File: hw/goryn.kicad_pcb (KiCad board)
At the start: 2 copper layers, 50 x 50 mm, 15 parts, among them J1 Conn_01x34, J2 Conn_01x34, J3 Conn_01x34, J4 Conn_01x34, U2 W25Q128JVS

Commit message: added DC-DC
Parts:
- added C1: 10uF, AI6YP:C_0603_1608Metric, F.Cu at (54.0, 89.5)
- added C10: 22uF, AI6YP:C_0603_1608Metric, F.Cu at (82.5, 81.4)
- added C11: 22uF, AI6YP:C_0603_1608Metric, F.Cu at (81.6, 67.4)
- added C12: 22uF, AI6YP:C_0603_1608Metric, F.Cu at (83.1, 69.0)
- added C2: 22uF, AI6YP:C_0603_1608Metric, F.Cu at (57.8, 89.4)
- added C3: 10uF, AI6YP:C_0603_1608Metric, F.Cu at (89.8, 94.8)
- added C4: 22uF, AI6YP:C_0603_1608Metric, F.Cu at (89.7, 91.2)
- added C5: 22uF, AI6YP:C_0603_1608Metric, F.Cu at (68.3, 67.7)
- added C6: 22uF, AI6YP:C_0603_1608Metric, F.Cu at (67.0, 69.0)
- added C7: 22uF, AI6YP:C_0603_1608Metric, F.Cu at (67.0, 81.5)
- added C8: 22uF, AI6YP:C_0603_1608Metric, F.Cu at (68.6, 83.0)
- added C9: 22uF, AI6YP:C_0603_1608Metric, F.Cu at (80.9, 82.8)
- added L1: 2.2uH, AI6YP:L_0805_2012Metric_Pad1.05x1.20mm_HandSolder, F.Cu at (60.3, 91.8)
- added L2: 2.2uH, AI6YP:L_0805_2012Metric_Pad1.05x1.20mm_HandSolder, F.Cu at (92.2, 89.8)
- added R10: 68K, AI6YP:R_0603_1608Metric, F.Cu at (57.6, 96.5)
- added R11: 15K, AI6YP:R_0603_1608Metric, F.Cu at (54.1, 96.4)
- added R12: 10K, AI6YP:R_0603_1608Metric, F.Cu at (96.5, 91.1)
- added R13: 15K, AI6YP:R_0603_1608Metric, F.Cu at (96.5, 94.7)
- added U3: MT3520B, AI6YP:SOT-23-5, F.Cu at (55.9, 92.7)
- added U4: MT3520B, AI6YP:SOT-23-5, F.Cu at (93.2, 94.1)
- moved R1 1.08 mm to (83.8, 80.1), turned to 135 degrees

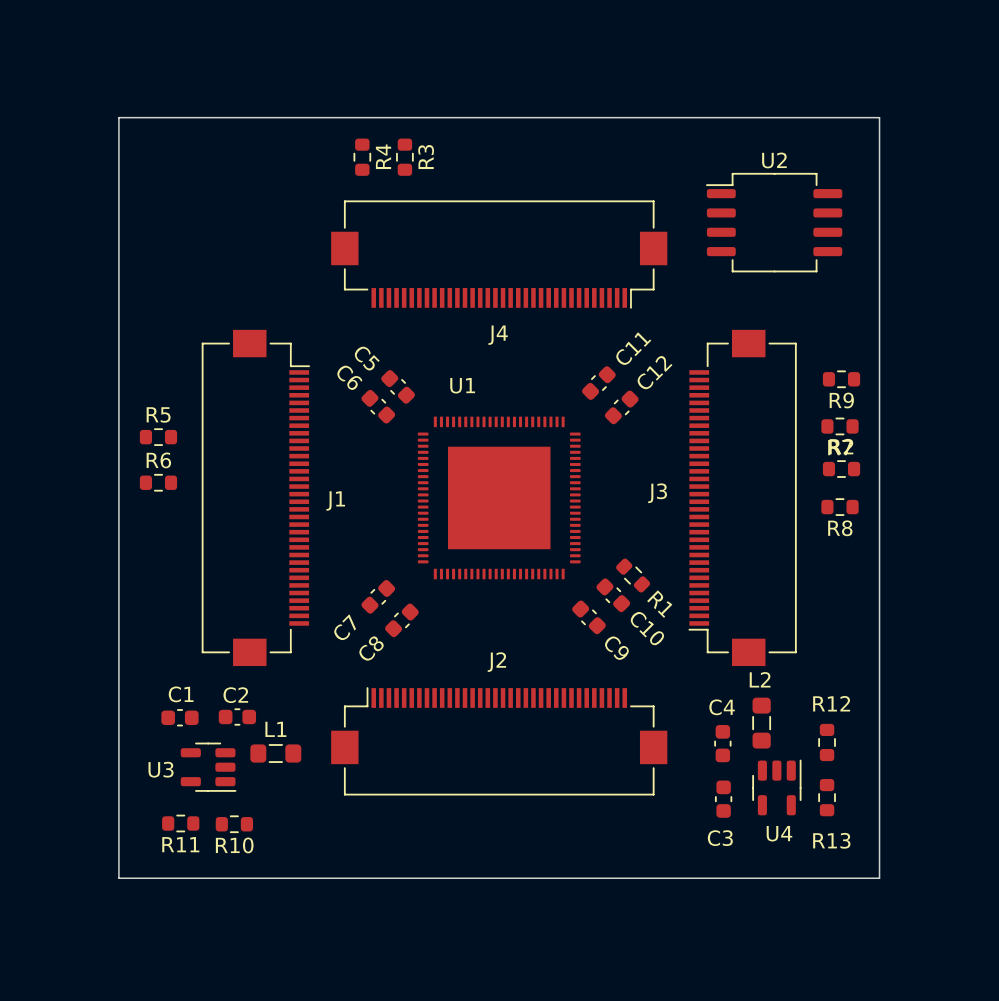
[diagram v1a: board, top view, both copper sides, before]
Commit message: FFC34 -> FFC30
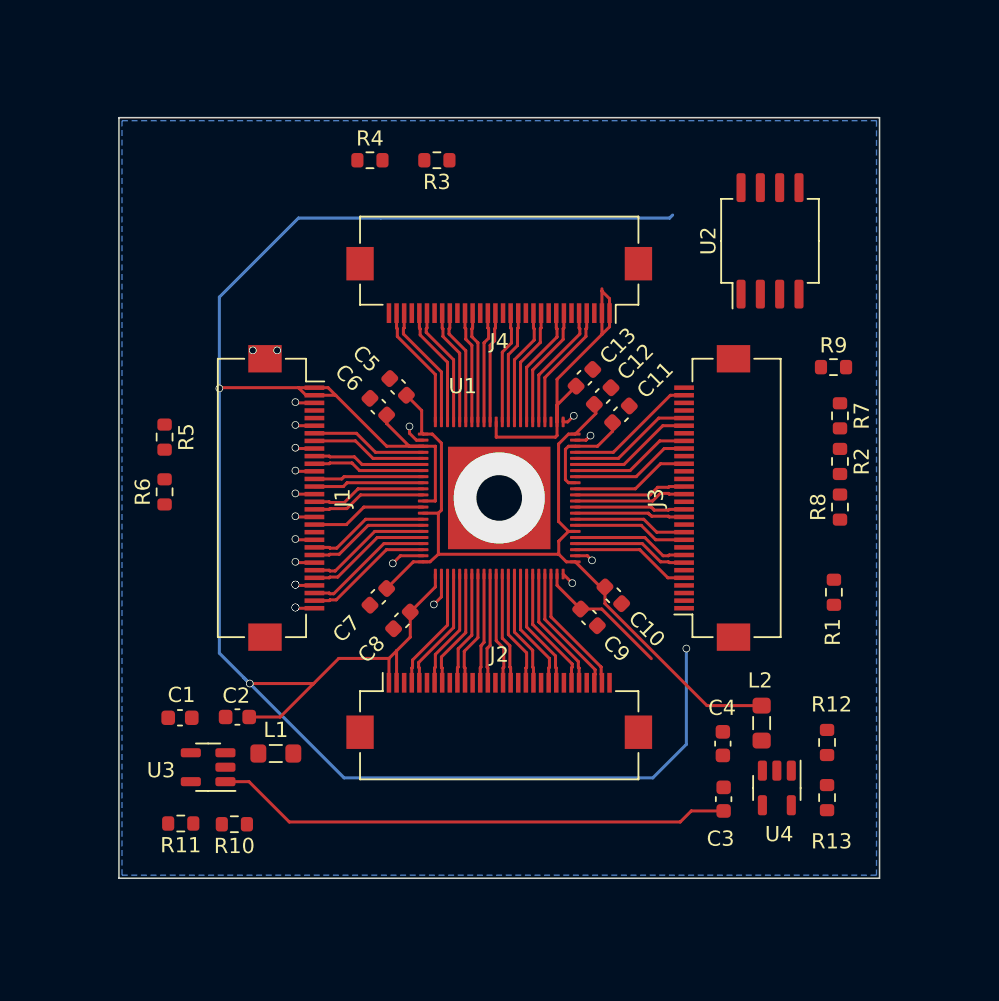
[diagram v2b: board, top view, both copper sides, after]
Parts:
- added C13: 22uF, AI6YP:C_0603_1608Metric, F.Cu at (80.6, 67.1)
- J1, J2, J3, J4: value Conn_01x34 -> Conn_FFC_30; footprint AI6YP:Hirose_FH12-34S-0.5SH_1x34-1MP_P0.50mm_Horizontal -> AI6YP:Hirose_FH12-30S-0.5SH_1x30-1MP_P0.50mm_Horizontal
- moved R1 13.2 mm to (97.0, 81.2), turned to 90 degrees
- moved C11 2.51 mm to (83.0, 69.5)
- moved R3 2.11 mm to (70.9, 52.8), turned to 180 degrees
- moved C12 1.46 mm to (81.8, 68.3)
- moved U2 1.24 mm to (92.8, 58.1), turned to 90 degrees
- moved J1 1.00 mm to (61.0, 75.0)
- moved J2 1.00 mm to (75.0, 89.0)
- moved J3 1.00 mm to (89.0, 75.0)
- moved J4 1.00 mm to (75.0, 61.0)
- moved R9 0.96 mm to (97.0, 66.4), turned to 0 degrees
- moved R6 0.72 mm to (53.0, 74.6), turned to 90 degrees
- moved R7 0.70 mm to (97.4, 69.6), turned to -90 degrees
- moved R4 0.54 mm to (66.5, 52.8), turned to 0 degrees
- moved R2 0.51 mm to (97.4, 72.6), turned to -90 degrees
- moved R5 0.40 mm to (53.0, 71.0), turned to -90 degrees
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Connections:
- J1 pad 1: GND -> +3V3
- J1 pad 10: GND -> /West/IOR26_P
- J1 pad 11: Net-(J1-Pin_11) -> /West/IOR26_N
- J1 pad 12: Net-(J1-Pin_12) -> GND
- J1 pad 13: GND -> Net-(J1-Pin_13)
- J1 pad 15: Net-(J1-Pin_15) -> GND
- J1 pad 16: GND -> /West/IOL29_P
- J1 pad 17: Net-(J1-Pin_17) -> /West/IOL29_N
- J1 pad 18: Net-(J1-Pin_18) -> GND
- J1 pad 19: GND -> Net-(J1-Pin_19)
- J1 pad 2: unconnected-(J1-Pin_2-Pad2) -> +3V3
- J1 pad 20: Net-(J1-Pin_20) -> unconnected-(J1-Pin_20-Pad20)
- J1 pad 21: unconnected-(J1-Pin_21-Pad21) -> GND
- J1 pad 22: GND -> /West/IOL47_P
- J1 pad 23: Net-(J1-Pin_23) -> /West/IOL47_N
- J1 pad 24: Net-(J1-Pin_24) -> GND
- J1 pad 25: GND -> /West/IOL49_P
- J1 pad 26: Net-(J1-Pin_26) -> /West/IOL49_N
- J1 pad 27: Net-(J1-Pin_27) -> GND
- J1 pad 28: GND -> /West/IOL51_P
- J1 pad 29: Net-(J1-Pin_29) -> /West/IOL51_N
- J1 pad 3: unconnected-(J1-Pin_3-Pad3) -> GND
- J1 pad 30: Net-(J1-Pin_30) -> GND
- J1 pad 4: GND -> unconnected-(J1-Pin_4-Pad4)
- J1 pad 6: unconnected-(J1-Pin_6-Pad6) -> GND
- J1 pad 7: GND -> Net-(J1-Pin_7)
- J1 pad 9: Net-(J1-Pin_9) -> GND
- J2 pad 1: GND -> +3V3
- J2 pad 10: GND -> /South/IOB14_P
- J2 pad 11: Net-(J2-Pin_11) -> /South/IOB14_N
- J2 pad 12: Net-(J2-Pin_12) -> GND
- J2 pad 13: GND -> /South/IOB18_P
- J2 pad 14: Net-(J2-Pin_14) -> /South/IOB18_N
- J2 pad 15: Net-(J2-Pin_15) -> GND
- J2 pad 16: GND -> /South/IOB24_P
- J2 pad 17: Net-(J2-Pin_17) -> /South/IOB24_N
- J2 pad 18: Net-(J2-Pin_18) -> GND
- J2 pad 19: GND -> /South/IOB30_P
- J2 pad 2: unconnected-(J2-Pin_2-Pad2) -> +3V3
- J2 pad 20: Net-(J2-Pin_20) -> /South/IOB30_N
- J2 pad 21: Net-(J2-Pin_21) -> GND
- J2 pad 22: GND -> /South/IOB34_P
- J2 pad 23: Net-(J2-Pin_23) -> /South/IOB34_N
- J2 pad 24: Net-(J2-Pin_24) -> GND
- J2 pad 25: GND -> /South/IOB40_P
- J2 pad 26: Net-(J2-Pin_26) -> /South/IOB40_N
- J2 pad 27: Net-(J2-Pin_27) -> GND
- J2 pad 28: GND -> /South/IOB43_P
- J2 pad 29: Net-(J2-Pin_29) -> /South/IOB43_N
- J2 pad 3: unconnected-(J2-Pin_3-Pad3) -> GND
- J2 pad 30: Net-(J2-Pin_30) -> GND
- J2 pad 4: GND -> /South/IOB6_P
- J2 pad 5: Net-(J2-Pin_5) -> /South/IOB6_N
- J2 pad 6: Net-(J2-Pin_6) -> GND
- J2 pad 7: GND -> /South/IOB8_P
- J2 pad 8: Net-(J2-Pin_8) -> /South/IOB8_N
- J2 pad 9: Net-(J2-Pin_9) -> GND
- J3 pad 1: GND -> +3V3
- J3 pad 10: GND -> Net-(J3-Pin_10)
- J3 pad 12: Net-(J3-Pin_12) -> GND
- J3 pad 13: GND -> /East/IOR38_N
- J3 pad 14: Net-(J3-Pin_14) -> /East/IOR38_P
- J3 pad 15: Net-(J3-Pin_15) -> GND
- J3 pad 16: GND -> /East/IOR36_N
- J3 pad 17: Net-(J3-Pin_17) -> /East/IOR36_P
- J3 pad 18: Net-(J3-Pin_18) -> GND
- J3 pad 19: GND -> unconnected-(J3-Pin_19-Pad19)
- J3 pad 2: unconnected-(J3-Pin_2-Pad2) -> +3V3
- J3 pad 20: unconnected-(J3-Pin_20-Pad20) -> MSPI_WP
- J3 pad 21: MSPI_WP -> GND
- J3 pad 22: GND -> MSPI_CLK
- J3 pad 23: MSPI_CLK -> MSPI_CS
- J3 pad 24: MSPI_CS -> GND
- J3 pad 25: GND -> MSPI_DI
- J3 pad 26: MSPI_DI -> MSPI_DO
- J3 pad 27: MSPI_DO -> GND
- J3 pad 28: GND -> unconnected-(J3-Pin_28-Pad28)
- J3 pad 29: unconnected-(J3-Pin_29-Pad29) -> MSPI_HOLD
- J3 pad 3: unconnected-(J3-Pin_3-Pad3) -> GND
- J3 pad 30: MSPI_HOLD -> GND
- J3 pad 4: GND -> unconnected-(J3-Pin_4-Pad4)
- J3 pad 5: unconnected-(J3-Pin_5-Pad5) -> Net-(J3-Pin_5)
- J3 pad 6: unconnected-(J3-Pin_6-Pad6) -> GND
- J3 pad 7: GND -> /East/IOR49_N
- J3 pad 8: Net-(J3-Pin_8) -> /East/IOR49_P
- J3 pad 9: Net-(J3-Pin_9) -> GND
- J4 pad 1: GND -> +3V3
- J4 pad 10: GND -> /North/IOT34_N
- J4 pad 11: Net-(J4-Pin_11) -> /North/IOT34_P
- J4 pad 12: Net-(J4-Pin_12) -> GND
- J4 pad 13: GND -> /North/IOT30_N
- J4 pad 14: Net-(J4-Pin_14) -> /North/IOT30_P
- J4 pad 15: Net-(J4-Pin_15) -> GND
- J4 pad 16: GND -> /North/IOT27_N
- J4 pad 17: Net-(J4-Pin_17) -> /North/IOT27_P
- J4 pad 18: Net-(J4-Pin_18) -> GND
- J4 pad 19: GND -> /North/IOT17_N
- J4 pad 2: unconnected-(J4-Pin_2-Pad2) -> +3V3
- J4 pad 20: Net-(J4-Pin_20) -> /North/IOT17_P
- J4 pad 21: Net-(J4-Pin_21) -> GND
- J4 pad 22: GND -> /North/IOT6_N
- J4 pad 23: Net-(J4-Pin_23) -> /North/IOT6_P
- J4 pad 24: Net-(J4-Pin_24) -> GND
- J4 pad 25: GND -> /North/IOT4_N
- J4 pad 26: Net-(J4-Pin_26) -> /North/IOT4_P
- J4 pad 27: Net-(J4-Pin_27) -> GND
- J4 pad 28: GND -> /North/IOR30_N
- J4 pad 29: Net-(J4-Pin_29) -> /North/IOR30_P
- J4 pad 3: unconnected-(J4-Pin_3-Pad3) -> GND
- J4 pad 30: Net-(J4-Pin_30) -> GND
- J4 pad 4: GND -> /North/IOT44_N
- J4 pad 5: unconnected-(J4-Pin_5-Pad5) -> /North/IOT44_P
- J4 pad 6: Net-(J4-Pin_6) -> GND
- J4 pad 7: GND -> /North/IOT40_N
- J4 pad 8: Net-(J4-Pin_8) -> /North/IOT40_P
- J4 pad 9: Net-(J4-Pin_9) -> GND
- R1 pad 2: Net-(U1C-EXTR) -> Net-(J3-Pin_5)
- R3 pad 2: Net-(J4-Pin_32) -> /North/IOR30_N
- R4 pad 2: Net-(J4-Pin_33) -> /North/IOR30_P
- R5 pad 2: Net-(J1-Pin_11) -> /West/IOR26_P
- R6 pad 2: Net-(J1-Pin_14) -> Net-(J1-Pin_13)
- U1 pad 10: Net-(J1-Pin_17) -> /West/IOL29_P
- U1 pad 11: Net-(J1-Pin_18) -> /West/IOL29_N
- U1 pad 13: Net-(J1-Pin_20) -> Net-(J1-Pin_19)
- U1 pad 15: Net-(J1-Pin_23) -> /West/IOL47_P
- U1 pad 16: Net-(J1-Pin_24) -> /West/IOL47_N
- U1 pad 17: Net-(J1-Pin_26) -> /West/IOL49_P
- U1 pad 18: Net-(J1-Pin_27) -> /West/IOL49_N
- U1 pad 19: Net-(J1-Pin_29) -> /West/IOL51_P
- U1 pad 20: Net-(J1-Pin_30) -> /West/IOL51_N
- U1 pad 25: Net-(J2-Pin_5) -> /South/IOB6_P
- U1 pad 26: Net-(J2-Pin_6) -> /South/IOB6_N
- U1 pad 27: Net-(J2-Pin_8) -> /South/IOB8_P
- U1 pad 28: Net-(J2-Pin_9) -> /South/IOB8_N
- U1 pad 29: Net-(J2-Pin_11) -> /South/IOB14_P
- U1 pad 30: Net-(J2-Pin_12) -> /South/IOB14_N
- U1 pad 31: Net-(J2-Pin_14) -> /South/IOB18_P
- U1 pad 32: Net-(J2-Pin_15) -> /South/IOB18_N
- U1 pad 33: Net-(J2-Pin_17) -> /South/IOB24_P
- U1 pad 34: Net-(J2-Pin_18) -> /South/IOB24_N
- U1 pad 35: Net-(J2-Pin_20) -> /South/IOB30_P
- U1 pad 36: Net-(J2-Pin_21) -> /South/IOB30_N
- U1 pad 37: Net-(J2-Pin_23) -> /South/IOB34_P
- U1 pad 38: Net-(J2-Pin_24) -> /South/IOB34_N
- U1 pad 39: Net-(J2-Pin_26) -> /South/IOB40_P
- U1 pad 4: Net-(J1-Pin_8) -> Net-(J1-Pin_7)
- U1 pad 40: Net-(J2-Pin_27) -> /South/IOB40_N
- U1 pad 41: Net-(J2-Pin_29) -> /South/IOB43_P
- U1 pad 42: Net-(J2-Pin_30) -> /South/IOB43_N
- U1 pad 43: GND -> +3V3
- U1 pad 44: +3V3 -> GND
- U1 pad 47: Net-(U1C-EXTR) -> Net-(J3-Pin_5)
- U1 pad 48: Net-(J3-Pin_8) -> /East/IOR49_N
- U1 pad 49: Net-(J3-Pin_9) -> /East/IOR49_P
- U1 pad 5: Net-(J1-Pin_9) -> Net-(J1-Pin_8)
- U1 pad 51: Net-(J3-Pin_11) -> Net-(J3-Pin_10)
- U1 pad 52: Net-(J3-Pin_12) -> Net-(J3-Pin_11)
- U1 pad 53: Net-(J3-Pin_14) -> /East/IOR38_N
- U1 pad 54: Net-(J3-Pin_15) -> /East/IOR38_P
- U1 pad 55: Net-(J3-Pin_17) -> /East/IOR36_N
- U1 pad 56: Net-(J3-Pin_18) -> /East/IOR36_P
- U1 pad 6: Net-(J1-Pin_11) -> /West/IOR26_P
- U1 pad 67: +3V3 -> GND
- U1 pad 68: GND -> +3V3
- U1 pad 69: Net-(J4-Pin_6) -> unconnected-(U1D-IOT50A-Pad69)
- U1 pad 7: Net-(J1-Pin_12) -> /West/IOR26_N
- U1 pad 70: Net-(J4-Pin_8) -> /North/IOT44_N
- U1 pad 71: Net-(J4-Pin_9) -> /North/IOT44_P
- U1 pad 72: Net-(J4-Pin_11) -> /North/IOT40_N
- U1 pad 73: Net-(J4-Pin_12) -> /North/IOT40_P
- U1 pad 74: Net-(J4-Pin_14) -> /North/IOT34_N
- U1 pad 75: Net-(J4-Pin_15) -> /North/IOT34_P
- U1 pad 76: Net-(J4-Pin_17) -> /North/IOT30_N
- U1 pad 77: Net-(J4-Pin_18) -> /North/IOT30_P
- U1 pad 79: Net-(J4-Pin_20) -> /North/IOT27_N
- U1 pad 8: Net-(J1-Pin_14) -> Net-(J1-Pin_13)
- U1 pad 80: Net-(J4-Pin_21) -> /North/IOT27_P
- U1 pad 81: Net-(J4-Pin_23) -> /North/IOT17_N
- U1 pad 82: Net-(J4-Pin_24) -> /North/IOT17_P
- U1 pad 83: Net-(J4-Pin_26) -> /North/IOT6_N
- U1 pad 84: Net-(J4-Pin_27) -> /North/IOT6_P
- U1 pad 85: Net-(J4-Pin_29) -> /North/IOT4_N
- U1 pad 86: Net-(J4-Pin_30) -> /North/IOT4_P
- U1 pad 87: Net-(J4-Pin_32) -> /North/IOR30_N
- U1 pad 88: Net-(J4-Pin_33) -> /North/IOR30_P
- U1 pad 9: Net-(J1-Pin_15) -> Net-(J1-Pin_14)
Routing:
- net +3V3: track 0.00 -> 187.2 mm, vias 0 -> 3
- net +1V0: track 0.00 -> 55.2 mm
- net +5V: track 0.00 -> 34.1 mm
- net GND: track 0.00 -> 23.5 mm, vias 0 -> 22
- net MSPI_HOLD: track 0.00 -> 8.70 mm
- net /South/IOB43_P: track 0.00 -> 8.54 mm
- net /South/IOB43_N: track 0.00 -> 8.54 mm
- net /West/IOL51_N: track 0.00 -> 8.54 mm
- net /West/IOL51_P: track 0.00 -> 8.54 mm
- net /North/IOT44_N: track 0.00 -> 8.29 mm
- net /North/IOT44_P: track 0.00 -> 8.29 mm
- net /South/IOB40_N: track 0.00 -> 8.25 mm
- net MSPI_DO: track 0.00 -> 8.25 mm
- net /West/IOL49_N: track 0.00 -> 8.25 mm
- net /South/IOB40_P: track 0.00 -> 8.25 mm
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- added copper zone on B.Cu, net GND
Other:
- rule pad_to_mask_clearance: 0 -> 0.04

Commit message: happy kicad 8
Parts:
- added C14: 1uF, AI6YP:C_0603_1608Metric, F.Cu at (63.4, 60.2)
- added H1: MountingHole_M3, AI6YP:MountingHole_3.2mm_M3_Pad_Via, F.Cu at (50.0, 75.0)
- added H2: MountingHole_M3, AI6YP:MountingHole_3.2mm_M3_Pad_Via, F.Cu at (75.0, 100.0)
- added H3: MountingHole_M3, AI6YP:MountingHole_3.2mm_M3_Pad_Via, F.Cu at (100.0, 75.0)
- added H4: MountingHole_M3, AI6YP:MountingHole_3.2mm_M3_Pad_Via, F.Cu at (75.0, 50.0)
- added J5: Conn_Coaxial, AI6YP:U.FL_Hirose_U.FL-R-SMT-1_Vertical, F.Cu at (53.4, 53.9)
- added J6: USB_C_Receptacle_USB2.0_16P, AI6YP:USB_C_Receptacle_GCT_USB4105-xx-A_16P_TopMnt_Horizontal, F.Cu at (56.4, 96.3)
- added R14: 22, AI6YP:R_0603_1608Metric, F.Cu at (56.7, 63.0)
- added R15: 22, AI6YP:R_0603_1608Metric, F.Cu at (53.4, 57.5)
- added R16: 0R, AI6YP:R_0603_1608Metric, F.Cu at (53.8, 84.6)
- added R17: 0R, AI6YP:R_0603_1608Metric, F.Cu at (52.2, 84.6)
- added R18: 5.1K, AI6YP:R_0603_1608Metric, F.Cu at (51.7, 89.7)
- added R19: 5.1K, AI6YP:R_0603_1608Metric, F.Cu at (63.7, 98.6)
- added X1: osc_4pin_3.2_2.5, AI6YP:Crystal_SMD_EuroQuartz_MT-4Pin_3.2x2.5mm_HandSoldering, F.Cu at (58.7, 58.5)
- moved R2 19.6 mm to (87.7, 55.6), turned to 90 degrees
- moved R1 13.0 mm to (84.1, 80.0), turned to 135 degrees
- moved R6 12.4 mm to (52.0, 62.2), turned to -90 degrees
- moved R9 11.8 mm to (87.7, 59.1), turned to -90 degrees
- moved R8 10.5 mm to (97.2, 65.1), turned to 180 degrees
- moved R11 9.61 mm to (63.7, 96.3), turned to 0 degrees
- moved R5 8.84 mm to (53.8, 62.2)
- moved R3 7.65 mm to (63.3, 52.2), turned to 0 degrees
- moved R7 7.62 mm to (96.8, 62.0), turned to 0 degrees
- moved C1 6.98 mm to (60.9, 90.4)
- moved R10 6.44 mm to (63.2, 93.3), turned to -90 degrees
- moved L1 4.90 mm to (61.3, 87.0)
- moved U3 4.46 mm to (56.6, 88.3)
- moved C2 3.59 mm to (61.3, 88.8)
- moved R4 3.41 mm to (63.3, 53.9)
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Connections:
- J1 pad 10: /West/IOR26_P -> /West/IOR26_N
- J1 pad 11: /West/IOR26_N -> GND
- J1 pad 12: GND -> Net-(J1-Pin_12)
- J1 pad 14: Net-(J1-Pin_14) -> GND
- J1 pad 15: GND -> /West/IOL29_P
- J1 pad 16: /West/IOL29_P -> /West/IOL29_N
- J1 pad 17: /West/IOL29_N -> GND
- J1 pad 18: GND -> Net-(J1-Pin_18)
- J1 pad 19: Net-(J1-Pin_19) -> unconnected-(J1-Pin_19-Pad19)
- J1 pad 2: +3V3 -> GND
- J1 pad 20: unconnected-(J1-Pin_20-Pad20) -> GND
- J1 pad 21: GND -> /West/IOL47_P
- J1 pad 22: /West/IOL47_P -> /West/IOL47_N
- J1 pad 23: /West/IOL47_N -> GND
- J1 pad 24: GND -> /West/IOL49_P
- J1 pad 25: /West/IOL49_P -> /West/IOL49_N
- J1 pad 26: /West/IOL49_N -> GND
- J1 pad 27: GND -> /West/IOL51_P
- J1 pad 28: /West/IOL51_P -> /West/IOL51_N
- J1 pad 29: /West/IOL51_N -> GND
- J1 pad 3: GND -> unconnected-(J1-Pin_3-Pad3)
- J1 pad 30: GND -> +3V3
- J1 pad 5: unconnected-(J1-Pin_5-Pad5) -> GND
- J1 pad 6: GND -> Net-(J1-Pin_6)
- J1 pad 8: Net-(J1-Pin_8) -> GND
- J1 pad 9: GND -> /West/IOR26_P
- J2 pad 10: /South/IOB14_P -> /South/IOB14_N
- J2 pad 11: /South/IOB14_N -> GND
- J2 pad 12: GND -> /South/IOB18_P
- J2 pad 13: /South/IOB18_P -> /South/IOB18_N
- J2 pad 14: /South/IOB18_N -> GND
- J2 pad 15: GND -> /South/IOB24_P
- J2 pad 16: /South/IOB24_P -> /South/IOB24_N
- J2 pad 17: /South/IOB24_N -> GND
- J2 pad 18: GND -> /South/IOB30_P
- J2 pad 19: /South/IOB30_P -> /South/IOB30_N
- J2 pad 2: +3V3 -> GND
- J2 pad 20: /South/IOB30_N -> GND
- J2 pad 21: GND -> /South/IOB34_P
- J2 pad 22: /South/IOB34_P -> /South/IOB34_N
- J2 pad 23: /South/IOB34_N -> GND
- J2 pad 24: GND -> /South/IOB40_P
- J2 pad 25: /South/IOB40_P -> /South/IOB40_N
- J2 pad 26: /South/IOB40_N -> GND
- J2 pad 27: GND -> /South/IOB43_P
- J2 pad 28: /South/IOB43_P -> /South/IOB43_N
- J2 pad 29: /South/IOB43_N -> GND
- J2 pad 3: GND -> /South/IOB6_P
- J2 pad 30: GND -> +3V3
- J2 pad 4: /South/IOB6_P -> /South/IOB6_N
- J2 pad 5: /South/IOB6_N -> GND
- J2 pad 6: GND -> /South/IOB8_P
- J2 pad 7: /South/IOB8_P -> /South/IOB8_N
- J2 pad 8: /South/IOB8_N -> GND
- J2 pad 9: GND -> /South/IOB14_P
- J3 pad 11: Net-(J3-Pin_11) -> GND
- J3 pad 12: GND -> /East/IOR38_N
- J3 pad 13: /East/IOR38_N -> /East/IOR38_P
- J3 pad 14: /East/IOR38_P -> GND
- J3 pad 15: GND -> /East/IOR36_N
- J3 pad 16: /East/IOR36_N -> /East/IOR36_P
- J3 pad 17: /East/IOR36_P -> GND
- J3 pad 18: GND -> unconnected-(J3-Pin_18-Pad18)
- J3 pad 19: unconnected-(J3-Pin_19-Pad19) -> MSPI_WP
- J3 pad 2: +3V3 -> GND
- J3 pad 20: MSPI_WP -> GND
- J3 pad 21: GND -> MSPI_CLK
- J3 pad 22: MSPI_CLK -> MSPI_CS
- J3 pad 23: MSPI_CS -> GND
- J3 pad 24: GND -> MSPI_DI
- J3 pad 25: MSPI_DI -> MSPI_DO
- J3 pad 26: MSPI_DO -> GND
- J3 pad 27: GND -> unconnected-(J3-Pin_27-Pad27)
- J3 pad 28: unconnected-(J3-Pin_28-Pad28) -> MSPI_HOLD
- J3 pad 29: MSPI_HOLD -> GND
- J3 pad 3: GND -> unconnected-(J3-Pin_3-Pad3)
- J3 pad 30: GND -> +3V3
- J3 pad 5: Net-(J3-Pin_5) -> GND
- J3 pad 6: GND -> /East/IOR49_N
- J3 pad 7: /East/IOR49_N -> /East/IOR49_P
- J3 pad 8: /East/IOR49_P -> GND
- J3 pad 9: GND -> Net-(J3-Pin_9)
- J4 pad 10: /North/IOT34_N -> /North/IOT34_P
- J4 pad 11: /North/IOT34_P -> GND
- J4 pad 12: GND -> /North/IOT30_N
- J4 pad 13: /North/IOT30_N -> /North/IOT30_P
- J4 pad 14: /North/IOT30_P -> GND
- J4 pad 15: GND -> /North/IOT27_N
- J4 pad 16: /North/IOT27_N -> /North/IOT27_P
- J4 pad 17: /North/IOT27_P -> GND
- J4 pad 18: GND -> /North/IOT17_N
- J4 pad 19: /North/IOT17_N -> /North/IOT17_P
- J4 pad 2: +3V3 -> GND
- J4 pad 20: /North/IOT17_P -> GND
- J4 pad 21: GND -> /North/IOT6_N
- J4 pad 22: /North/IOT6_N -> /North/IOT6_P
- J4 pad 23: /North/IOT6_P -> GND
- J4 pad 24: GND -> /North/IOT4_N
- J4 pad 25: /North/IOT4_N -> /North/IOT4_P
- J4 pad 26: /North/IOT4_P -> GND
- J4 pad 27: GND -> /North/IOR30_N
- J4 pad 28: /North/IOR30_N -> /North/IOR30_P
- J4 pad 29: /North/IOR30_P -> GND
- J4 pad 3: GND -> /North/IOT44_N
- J4 pad 30: GND -> +3V3
- J4 pad 4: /North/IOT44_N -> /North/IOT44_P
- J4 pad 5: /North/IOT44_P -> GND
- J4 pad 6: GND -> /North/IOT40_N
- J4 pad 7: /North/IOT40_N -> /North/IOT40_P
- J4 pad 8: /North/IOT40_P -> GND
- J4 pad 9: GND -> /North/IOT34_N
- R1 pad 2: Net-(J3-Pin_5) -> Net-(U1C-EXTR)
- R6 pad 2: Net-(J1-Pin_13) -> Net-(J1-Pin_12)
- U1 pad 13: Net-(J1-Pin_19) -> Net-(J1-Pin_18)
- U1 pad 4: Net-(J1-Pin_7) -> Net-(J1-Pin_6)
- U1 pad 43: +3V3 -> GND
- U1 pad 44: GND -> +3V3
- U1 pad 47: Net-(J3-Pin_5) -> Net-(U1C-EXTR)
- U1 pad 5: Net-(J1-Pin_8) -> Net-(J1-Pin_7)
- U1 pad 51: Net-(J3-Pin_10) -> Net-(J3-Pin_9)
- U1 pad 52: Net-(J3-Pin_11) -> Net-(J3-Pin_10)
- U1 pad 67: GND -> +3V3
- U1 pad 68: +3V3 -> GND
- U1 pad 8: Net-(J1-Pin_13) -> Net-(J1-Pin_12)
- U1 pad 9: Net-(J1-Pin_14) -> Net-(J1-Pin_13)
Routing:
- net MSPI_CLK: track 7.92 -> 42.9 mm
- net GND: track 23.5 -> 57.9 mm, vias 22 -> 42
- net +5V: track 34.1 -> 65.8 mm, vias 0 -> 3
- net MSPI_WP: track 7.83 -> 34.5 mm
- net Net-(J1-Pin_6): track 0.00 -> 24.7 mm
- net Net-(J1-Pin_12): track 0.00 -> 23.2 mm
- net MSPI_DI: track 8.21 -> 31.3 mm, vias 0 -> 2
- net MSPI_DO: track 8.25 -> 28.9 mm
- net MSPI_CS: track 7.96 -> 27.4 mm
- net MSPI_HOLD: track 8.70 -> 28.0 mm
- net /West/IOR26_P: track 7.38 -> 21.3 mm
- net /North/IOR30_N: track 8.21 -> 21.7 mm
- net Net-(J6-D+-PadA6): track 0.00 -> 13.4 mm
- net /North/IOR30_P: track 8.21 -> 20.4 mm
- net /West/IOL51_P: track 8.54 -> 20.6 mm
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- added copper zone on F.Cu, net GND

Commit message: finished routing
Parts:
- removed C2, C4, C7: 22uF, AI6YP:C_0603_1608Metric
- removed C3: 10uF, AI6YP:C_0603_1608Metric
- removed H1, H2, H3, H4: MountingHole_M3, AI6YP:MountingHole_3.2mm_M3_Pad_Via
- removed L1, L2: 2.2uH, AI6YP:L_0805_2012Metric_Pad1.05x1.20mm_HandSolder
- removed R16, R17: 0R, AI6YP:R_0603_1608Metric
- removed R18, R19: 5.1K, AI6YP:R_0603_1608Metric
- added C31: 10uF, AI6YP:C_0603_1608Metric, F.Cu at (59.0, 98.5)
- added C32: 22uF, AI6YP:C_0603_1608Metric, F.Cu at (66.0, 84.0)
- added C41: 10uF, AI6YP:C_0603_1608Metric, F.Cu at (90.5, 96.3)
- added C42: 22uF, AI6YP:C_0603_1608Metric, F.Cu at (91.0, 87.5)
- added J10: 3V3, AI6YP:PinHeader_1x02_P2.54mm_Vertical, F.Cu at (52.0, 62.5)
- added J30: EMI-shield-clip-corner, AI6YP:EMI-shield-clip-corner, F.Cu at (51.0, 51.0)
- added J31: EMI-shield-clip-corner, AI6YP:EMI-shield-clip-corner, F.Cu at (51.0, 99.0)
- added J32: EMI-shield-clip-corner, AI6YP:EMI-shield-clip-corner, F.Cu at (99.0, 99.0)
- added J33: EMI-shield-clip-corner, AI6YP:EMI-shield-clip-corner, F.Cu at (99.0, 51.0)
- added J8: 5V, AI6YP:PinHeader_1x02_P2.54mm_Vertical, F.Cu at (87.5, 98.0)
- added J9: 1V, AI6YP:PinHeader_1x02_P2.54mm_Vertical, F.Cu at (98.0, 87.5)
- added L31: 2.2uH, AI6YP:L_0805_2012Metric_Pad1.05x1.20mm_HandSolder, F.Cu at (60.7, 87.5)
- added L41: 2.2uH, AI6YP:L_0805_2012Metric_Pad1.05x1.20mm_HandSolder, F.Cu at (87.5, 89.0)
- added R31: 68K, AI6YP:R_0603_1608Metric, F.Cu at (63.6, 90.2)
- added R32: 15K, AI6YP:R_0603_1608Metric, F.Cu at (63.6, 93.7)
- added R41: 10K, AI6YP:R_0603_1608Metric, F.Cu at (95.5, 92.0)
- added R42: 15K, AI6YP:R_0603_1608Metric, F.Cu at (95.5, 95.5)
- C1: value 10uF -> 22uF
- R10: value 68K -> 5.1K
- R11: value 15K -> 5.1K
- R12: value 10K -> 0R
- R13: value 15K -> 0R
- moved R12 36.3 mm to (60.5, 95.5), turned to 0 degrees
- moved R13 36.1 mm to (60.5, 97.0), turned to 0 degrees
- moved R11 15.8 mm to (53.5, 84.2), turned to 90 degrees
- moved R10 12.3 mm to (55.0, 84.2), turned to 90 degrees
- moved C1 11.6 mm to (67.0, 80.5), turned to -135 degrees
- moved R8 7.24 mm to (90.3, 63.0), turned to 0 degrees
- moved R7 6.59 mm to (90.3, 61.1)
- moved R15 6.47 mm to (58.5, 61.5), turned to -90 degrees
- moved J6 5.88 mm to (53.0, 91.5), turned to -90 degrees
- moved U3 5.59 mm to (61.0, 91.7), turned to -90 degrees
- moved R5 5.22 mm to (55.3, 67.2)
- moved R6 5.22 mm to (53.5, 67.2)
- moved X1 4.52 mm to (60.6, 54.4)
- moved R14 4.11 mm to (60.5, 61.5), turned to -90 degrees
- moved J5 3.18 mm to (54.0, 57.0), turned to 180 degrees
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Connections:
- net /South/IOB43_N renamed Net-(J2-Pin_28)
- net /South/IOB43_P renamed Net-(J2-Pin_27)
- C1 pad 1: +5V -> +1V0
- J3 pad 18: unconnected-(J3-Pin_18-Pad18) -> MSPI_WP
- J3 pad 19: MSPI_WP -> unconnected-(J3-Pin_19-Pad19)
- R10 pad 1: +3V3 -> Net-(J6-CC1)
- R10 pad 2: Net-(U3-FB) -> GND
- R11 pad 1: Net-(U3-FB) -> Net-(J6-CC2)
- R12 pad 1: +1V0 -> Net-(J6-D--PadA7)
- R12 pad 2: Net-(U4-FB) -> /South/IOB6_P
- R13 pad 1: Net-(U4-FB) -> Net-(J6-D+-PadA6)
- R13 pad 2: GND -> /South/IOB6_N
- R15 pad 1: Net-(J1-Pin_6) -> Net-(J5-In)
- R15 pad 2: Net-(J5-In) -> Net-(J1-Pin_6)
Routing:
- net GND: track 57.9 -> 2.40 mm, vias 42 -> 178
- net +5V: track 65.8 -> 15.9 mm, vias 3 -> 8
- net +3V3: track 199.2 -> 150.6 mm, vias 12 -> 14
- net /South/IOB6_N: track 8.33 -> 23.6 mm
- net /South/IOB6_P: track 8.33 -> 23.4 mm
- net /West/IOL51_P: track 20.6 -> 8.33 mm
- net /West/IOL51_N: track 19.3 -> 8.33 mm
- net MSPI_WP: track 34.5 -> 43.2 mm, vias 0 -> 2
- net Net-(U3-FB): track 10.7 -> 3.69 mm
- net MSPI_CLK: track 42.9 -> 48.9 mm
- net MSPI_CS: track 27.4 -> 32.7 mm, vias 0 -> 2
- net Net-(J5-In): track 0.00 -> 5.34 mm
- net MSPI_HOLD: track 28.0 -> 32.6 mm
- net /West/IOR26_P: track 21.3 -> 17.1 mm
- net Net-(J1-Pin_12): track 23.2 -> 19.2 mm
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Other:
- outline, holes or cut-outs redrawn
- board text added: "A"
- board text added: "EU2A I6YP"
- board text added: "ГОРЫНЬ V1.0.0"
